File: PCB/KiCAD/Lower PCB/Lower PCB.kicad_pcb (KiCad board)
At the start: 2 copper layers, 179.5 x 163.2 mm, 138 parts, among them IC1 ADG608BRZ, IC2 ADG608BRZ, J1 Conn_01x04, J2 Conn_01x02, J3 Conn_01x08, M1 Conn_01x02_Pin, M2 Conn_01x02_Pin, M3 Conn_01x02_Pin, M4 Conn_01x02_Pin, Q1 SFH320, Q10 SFH320, Q11 SFH320, Q12 SFH320, Q13 SFH320, Q14 SFH320, Q15 SFH320, Q16 SFH320, Q2 SFH320, Q3 SFH320, Q4 SFH320, Q5 SFH320, Q6 SFH320, Q7 SFH320, Q8 SFH320, Q9 SFH320, U1 ATmega328PB-A, U2 LMD18200, U3 LMD18200, U4 LMD18200, U5 LMD18200, U6 ATmega328PB-A, Y1 Crystal_GND24, Y2 Crystal_GND24

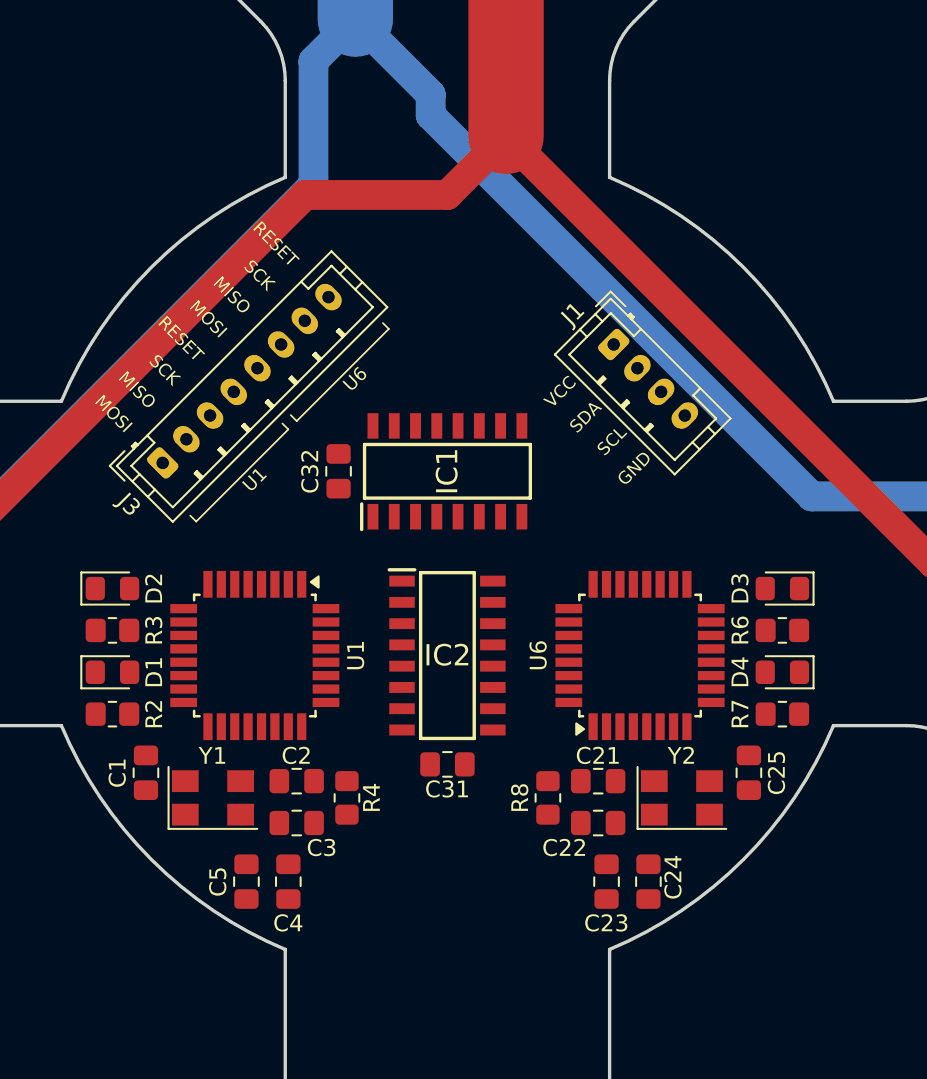
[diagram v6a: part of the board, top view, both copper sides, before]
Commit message: More work to the Main PCB and refinement of Via sizes
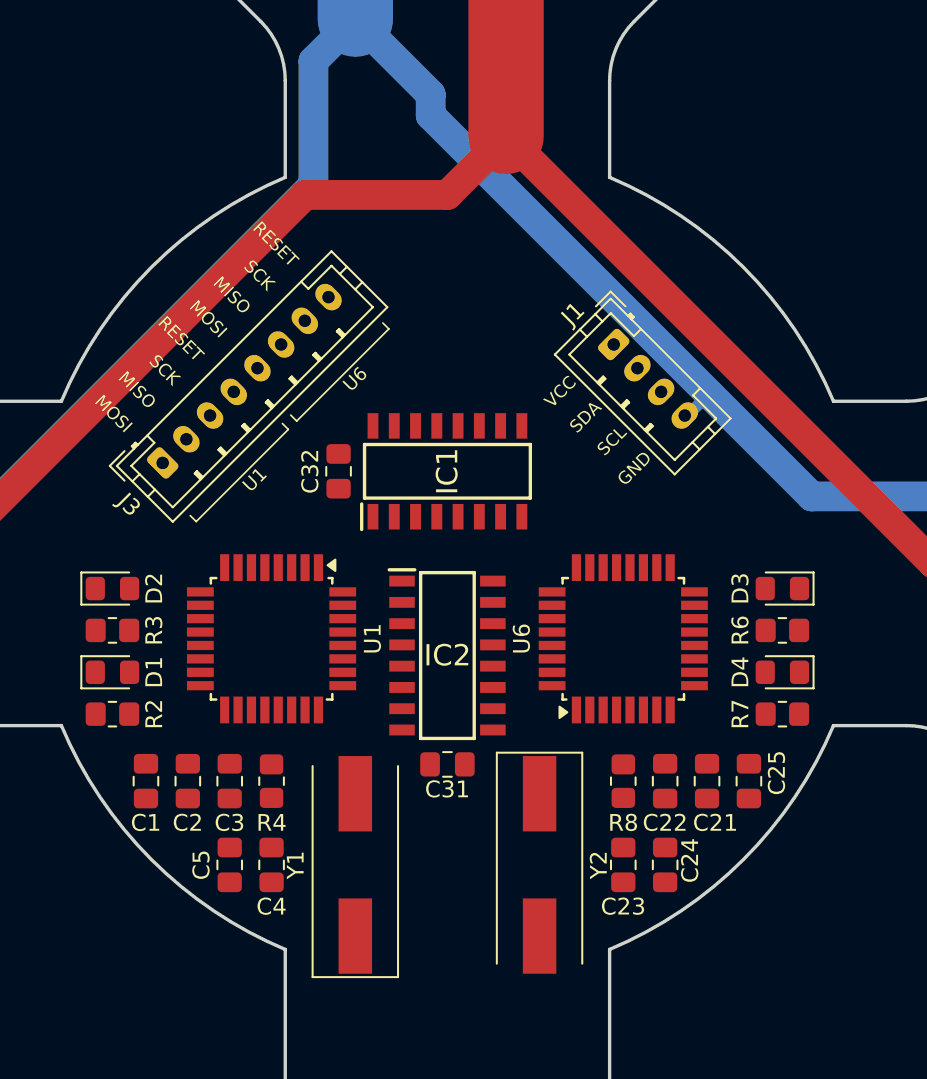
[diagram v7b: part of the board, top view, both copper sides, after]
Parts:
- Y1, Y2: value Crystal_GND24 -> Crystal; footprint Crystal:Crystal_SMD_5032-4Pin_5.0x3.2mm -> Crystal:Crystal_SMD_HC49-SD
- moved Y1 9.39 mm to (-5.50, 18.0), turned to 90 degrees
- moved Y2 9.39 mm to (5.50, 18.0), turned to -90 degrees
- moved C2 6.50 mm to (-15.5, 13.0), turned to 90 degrees
- moved C21 6.50 mm to (15.5, 13.0), turned to -90 degrees
- moved C22 4.72 mm to (13.0, 13.0), turned to -90 degrees
- moved C3 4.72 mm to (-13.0, 13.0), turned to -90 degrees
- moved R4 4.61 mm to (-10.5, 13.0)
- moved R8 4.61 mm to (10.5, 13.0)
- moved C23 1.41 mm to (10.5, 18.0)
- moved C24 1.41 mm to (13.0, 18.0)
- moved C4 1.41 mm to (-10.5, 18.0)
- moved C5 1.41 mm to (-13.0, 18.0)
- moved U1 1.41 mm to (-10.5, 4.50)
- moved U6 1.41 mm to (10.5, 4.50)
- moved C1 0.50 mm to (-18.0, 13.0)
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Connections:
- Y1 pad 1: Net-(U1-XTAL1/PB6) -> Net-(U1-XTAL2/PB7)
- Y1 pad 2: unconnected-(Y1-Pad2) -> Net-(U1-XTAL1/PB6)
- Y2 pad 1: Net-(U6-XTAL1/PB6) -> Net-(U6-XTAL2/PB7)
- Y2 pad 2: unconnected-(Y2-Pad2) -> Net-(U6-XTAL1/PB6)
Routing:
- net MOTOR_1_BRAKE: track 379.0 -> 381.0 mm

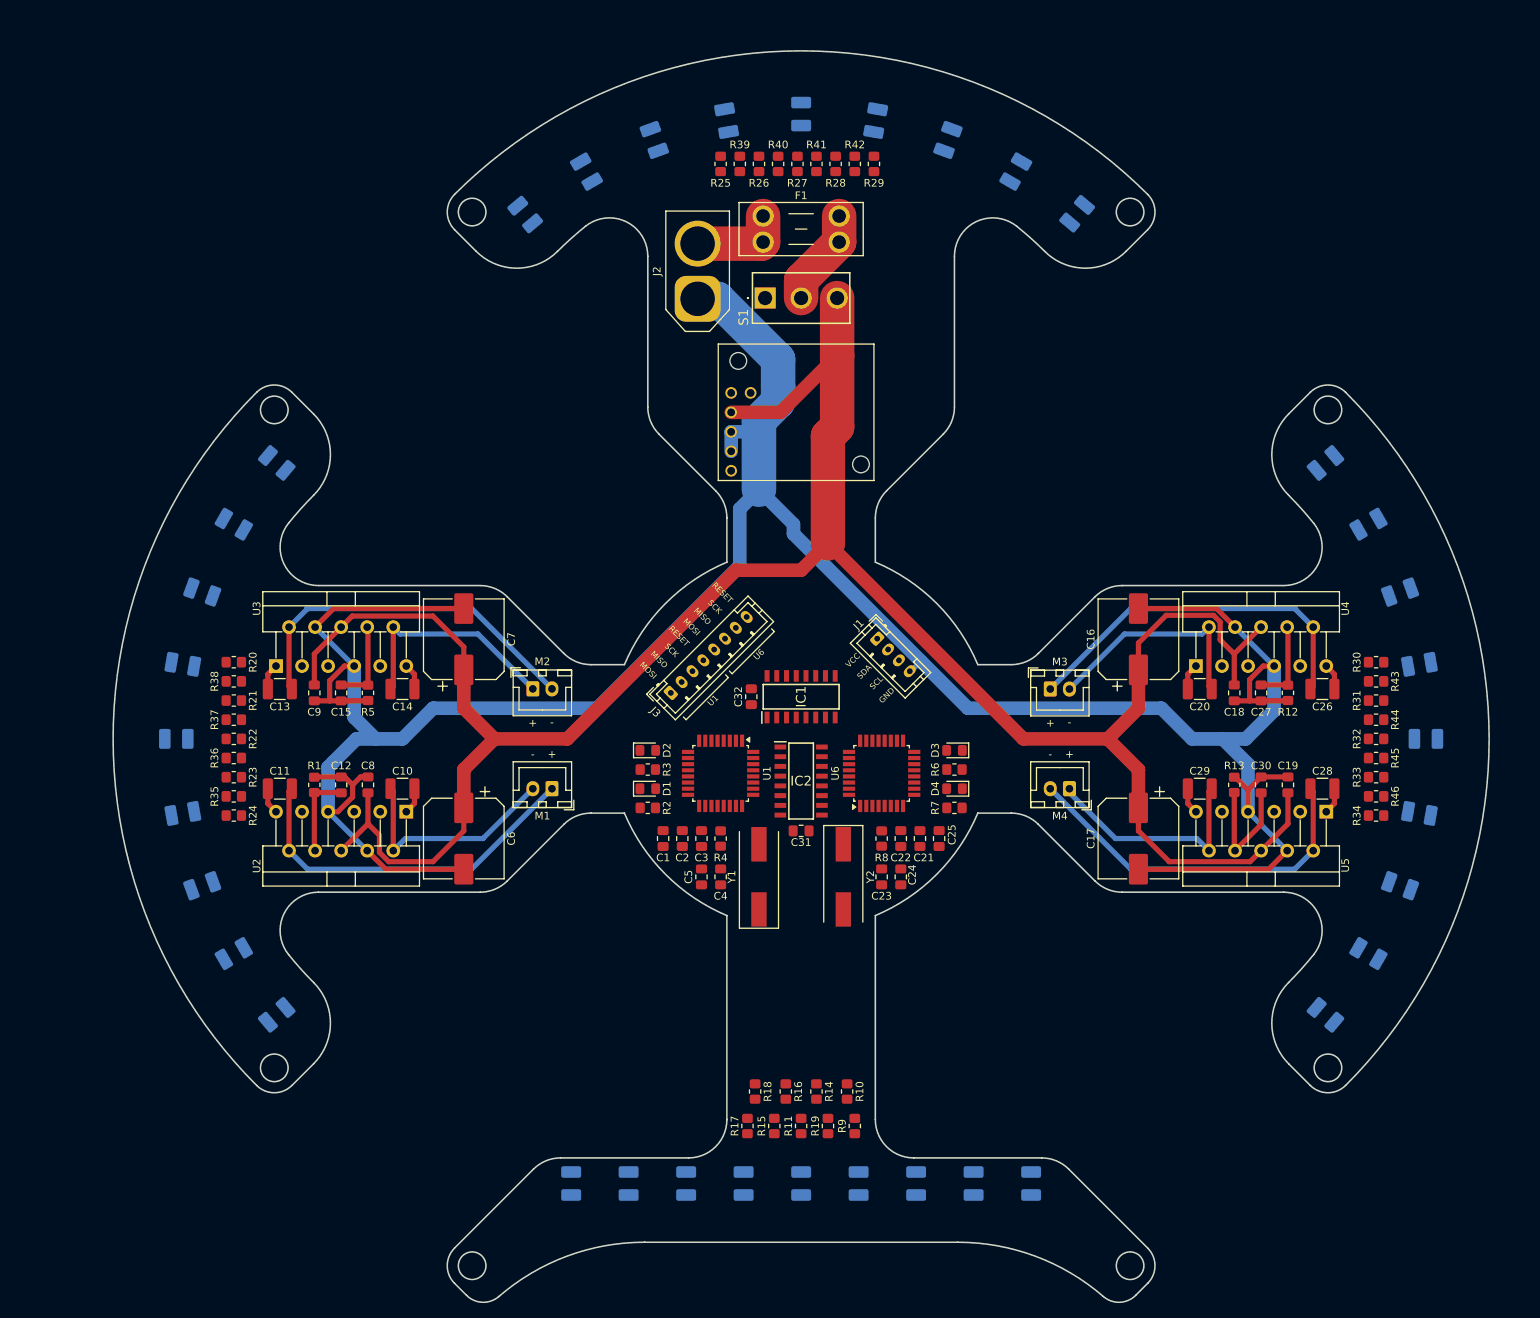
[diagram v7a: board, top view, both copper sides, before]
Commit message: Redone main PCB traces and started lower PCB
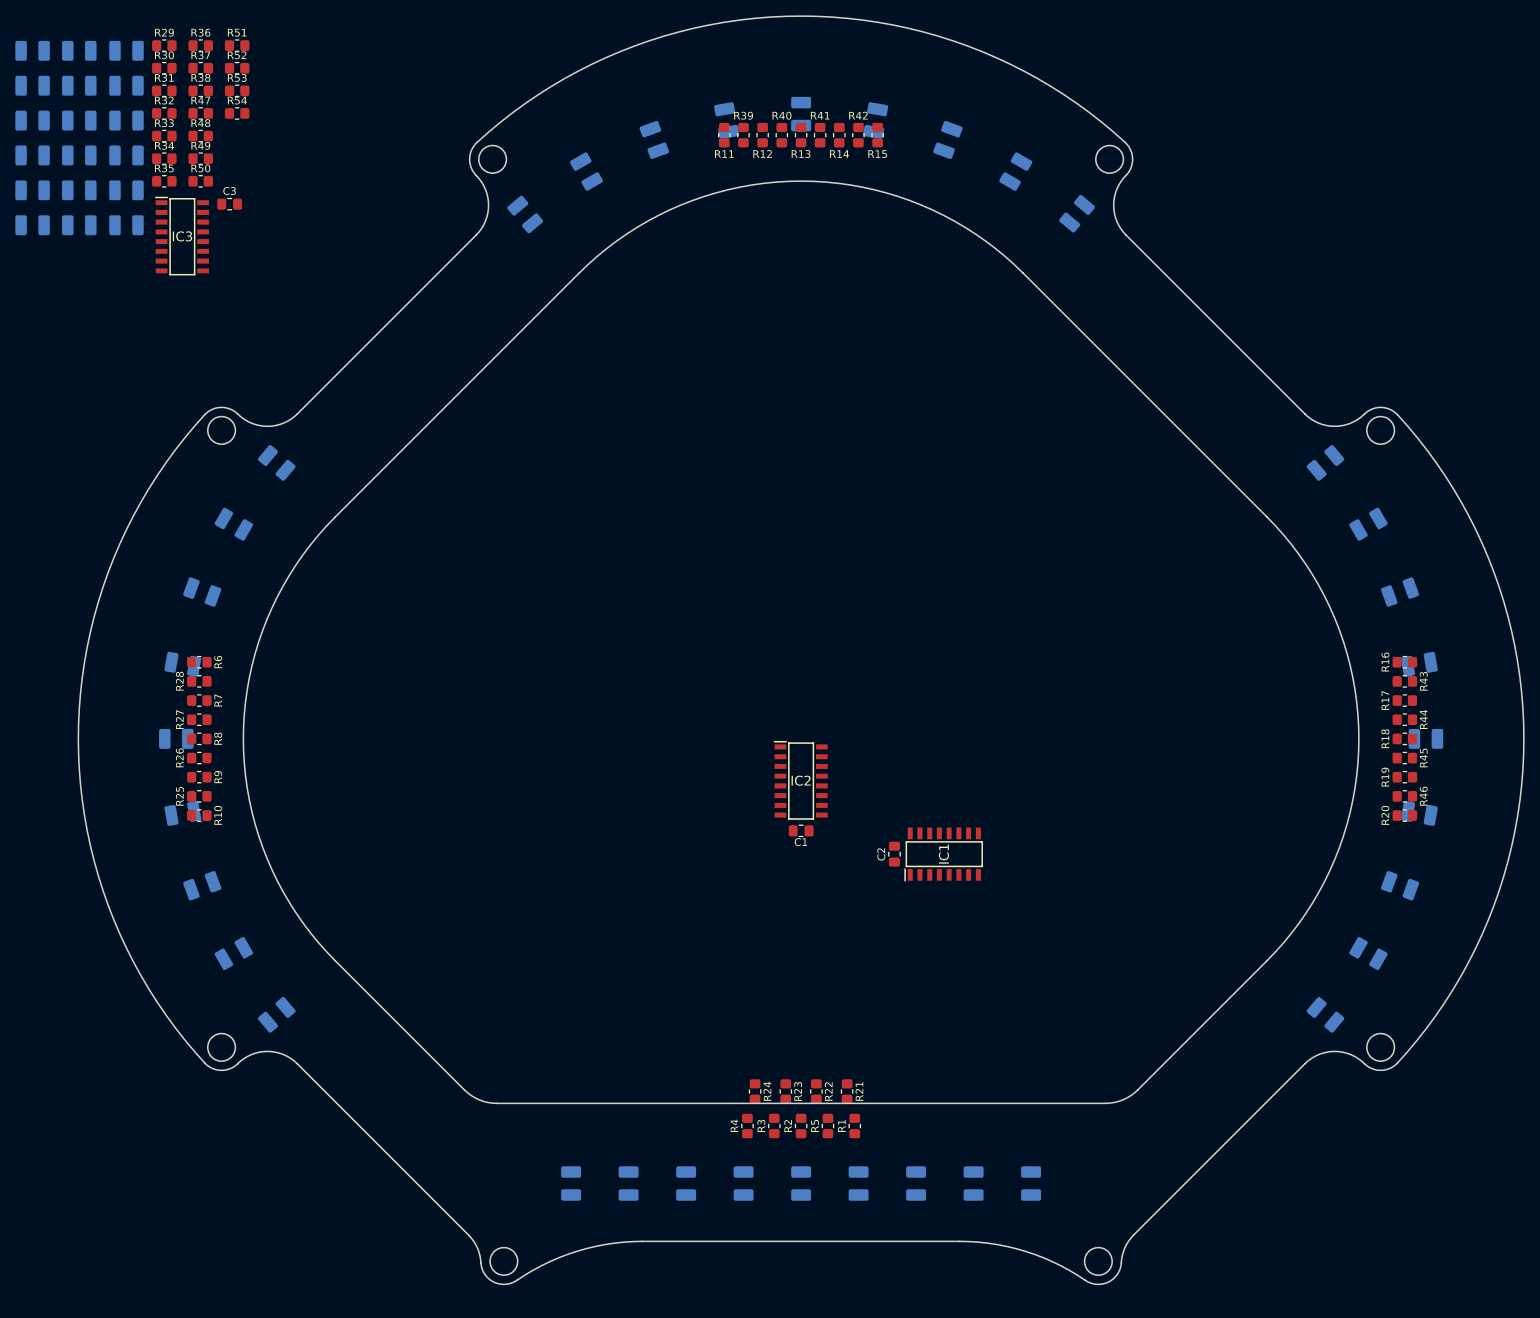
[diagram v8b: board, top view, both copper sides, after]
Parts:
- removed the C1 at (-18.0, 13.0)
- removed C10, C11, C13, C14, C20, C26, C28, C29: 10nF, Capacitor_SMD:C_1210_3225Metric_Pad1.33x2.70mm_HandSolder
- removed C12, C15, C18, C19, C27, C30, C8, C9: 0.1uF, Capacitor_SMD:C_0805_2012Metric_Pad1.18x1.45mm_HandSolder
- removed C16, C17, C6, C7: 220uF, Capacitor_SMD:CP_Elec_10x10
- removed the C2 at (-15.5, 13.0)
- removed C21, C22, C25: 100nF, Capacitor_SMD:C_0805_2012Metric_Pad1.18x1.45mm_HandSolder
- removed C23, C24, C4, C5: 22pF, Capacitor_SMD:C_0805_2012Metric_Pad1.18x1.45mm_HandSolder
- removed the D1 at (-20.0, 6.50)
- removed the D2 at (-20.0, 1.50)
- removed the D3 at (20.0, 1.50)
- removed the D4 at (20.0, 6.50)
- removed F1: Fuse, Fuse:Fuseholder_Blade_Mini_Keystone_3568
- removed J1: Conn_01x04, Connector_JST:JST_PH_B4B-PH-K_1x04_P2.00mm_Vertical
- removed J2: Conn_01x02, Connector_AMASS:AMASS_XT60-M_1x02_P7.20mm_Vertical
- removed J3: Conn_01x08, Connector_JST:JST_PH_B8B-PH-K_1x08_P2.00mm_Vertical
- removed M1, M2, M3, M4: Conn_01x02_Pin, Connector_JST:JST_XH_B2B-XH-A_1x02_P2.50mm_Vertical
- removed the R1 at (-63.5, 6.00)
- removed the R12 at (63.5, -6.00)
- removed the R13 at (56.5, 6.00)
- removed the R2 at (-20.0, 9.00)
- removed the R3 at (-20.0, 4.00)
- removed the R4 at (-10.5, 13.0)
- removed the R5 at (-56.5, -6.00)
- removed the R6 at (20.0, 4.00)
- removed the R7 at (20.0, 9.00)
- removed the R8 at (10.5, 13.0)
- removed S1: 1101M2S3CGE2, 1101M2S3CGE2:1101M2S3CGE2
- removed U1, U6: ATmega328PB-A, Package_QFP:TQFP-32_7x7mm_P0.8mm
- removed U2, U3, U4, U5: LMD18200, Package_TO_SOT_THT:TO-220-11_P3.4x5.08mm_StaggerOdd_Lead4.58mm_Vertical
- removed U7: ~, Pololu:D36V28F5
- removed Y1, Y2: Crystal, Crystal:Crystal_SMD_HC49-SD
- added D21: LED, LED_SMD:LED_PLCC-2_3.4x3.0mm_KA, B.Cu at (-94.2, -89.8)
- added D22: LED, LED_SMD:LED_PLCC-2_3.4x3.0mm_KA, B.Cu at (-94.2, -85.2)
- added D23: LED, LED_SMD:LED_PLCC-2_3.4x3.0mm_KA, B.Cu at (-94.2, -80.7)
- added D24: LED, LED_SMD:LED_PLCC-2_3.4x3.0mm_KA, B.Cu at (-94.2, -76.1)
- added D25: LED, LED_SMD:LED_PLCC-2_3.4x3.0mm_KA, B.Cu at (-94.2, -71.5)
- added D26: LED, LED_SMD:LED_PLCC-2_3.4x3.0mm_KA, B.Cu at (-94.2, -67.0)
- added D27: LED, LED_SMD:LED_PLCC-2_3.4x3.0mm_KA, B.Cu at (-100.2, -89.8)
- added D28: LED, LED_SMD:LED_PLCC-2_3.4x3.0mm_KA, B.Cu at (-100.2, -85.2)
- added D29: LED, LED_SMD:LED_PLCC-2_3.4x3.0mm_KA, B.Cu at (-100.2, -80.7)
- added D30: LED, LED_SMD:LED_PLCC-2_3.4x3.0mm_KA, B.Cu at (-100.2, -76.1)
- added IC3: ADG608BRZ, ADG608BRZ:SOIC127P600X175-16N, F.Cu at (-80.7, -65.5)
- added Q17: SFH320, LED_SMD:LED_PLCC-2_3.4x3.0mm_KA, B.Cu at (-100.2, -71.5)
- added Q18: SFH320, LED_SMD:LED_PLCC-2_3.4x3.0mm_KA, B.Cu at (-100.2, -67.0)
- added Q19: SFH320, LED_SMD:LED_PLCC-2_3.4x3.0mm_KA, B.Cu at (-88.0, -89.8)
- added Q20: SFH320, LED_SMD:LED_PLCC-2_3.4x3.0mm_KA, B.Cu at (-88.0, -85.2)
- added Q21: SFH320, LED_SMD:LED_PLCC-2_3.4x3.0mm_KA, B.Cu at (-88.0, -80.7)
- added Q22: SFH320, LED_SMD:LED_PLCC-2_3.4x3.0mm_KA, B.Cu at (-88.0, -76.1)
- added Q23: SFH320, LED_SMD:LED_PLCC-2_3.4x3.0mm_KA, B.Cu at (-88.0, -71.5)
- added Q24: SFH320, LED_SMD:LED_PLCC-2_3.4x3.0mm_KA, B.Cu at (-88.0, -67.0)
- added R29: 330, Resistor_SMD:R_0805_2012Metric_Pad1.20x1.40mm_HandSolder, F.Cu at (-83.1, -90.4)
- added R30: 330, Resistor_SMD:R_0805_2012Metric_Pad1.20x1.40mm_HandSolder, F.Cu at (-83.1, -87.5)
- added R31: 330, Resistor_SMD:R_0805_2012Metric_Pad1.20x1.40mm_HandSolder, F.Cu at (-83.1, -84.5)
- added R32: 330, Resistor_SMD:R_0805_2012Metric_Pad1.20x1.40mm_HandSolder, F.Cu at (-83.1, -81.6)
- added R33: 330, Resistor_SMD:R_0805_2012Metric_Pad1.20x1.40mm_HandSolder, F.Cu at (-83.1, -78.6)
- added R34: 330, Resistor_SMD:R_0805_2012Metric_Pad1.20x1.40mm_HandSolder, F.Cu at (-83.1, -75.7)
- added R35: 330, Resistor_SMD:R_0805_2012Metric_Pad1.20x1.40mm_HandSolder, F.Cu at (-83.1, -72.7)
- added R36: 330, Resistor_SMD:R_0805_2012Metric_Pad1.20x1.40mm_HandSolder, F.Cu at (-78.3, -90.4)
- added R37: 330, Resistor_SMD:R_0805_2012Metric_Pad1.20x1.40mm_HandSolder, F.Cu at (-78.3, -87.5)
- added R38: 330, Resistor_SMD:R_0805_2012Metric_Pad1.20x1.40mm_HandSolder, F.Cu at (-78.3, -84.5)
- added R47: 10k, Resistor_SMD:R_0805_2012Metric_Pad1.20x1.40mm_HandSolder, F.Cu at (-78.3, -81.6)
- added R48: 10k, Resistor_SMD:R_0805_2012Metric_Pad1.20x1.40mm_HandSolder, F.Cu at (-78.3, -78.6)
- added R49: 10k, Resistor_SMD:R_0805_2012Metric_Pad1.20x1.40mm_HandSolder, F.Cu at (-78.3, -75.7)
- added R50: 10k, Resistor_SMD:R_0805_2012Metric_Pad1.20x1.40mm_HandSolder, F.Cu at (-78.3, -72.7)
- added R51: 10k, Resistor_SMD:R_0805_2012Metric_Pad1.20x1.40mm_HandSolder, F.Cu at (-73.6, -90.4)
- added R52: 10k, Resistor_SMD:R_0805_2012Metric_Pad1.20x1.40mm_HandSolder, F.Cu at (-73.6, -87.5)
- added R53: 10k, Resistor_SMD:R_0805_2012Metric_Pad1.20x1.40mm_HandSolder, F.Cu at (-73.6, -84.5)
- added R54: 10k, Resistor_SMD:R_0805_2012Metric_Pad1.20x1.40mm_HandSolder, F.Cu at (-73.6, -81.6)
- moved C3 103.1 mm to (-74.5, -69.8), turned to 0 degrees
- moved C2 27.8 mm to (12.2, 15.0)
- moved IC1 27.8 mm to (18.7, 15.0)
- moved R10 4.50 mm to (-78.5, 10.0)
- moved R25 4.50 mm to (-78.5, 7.50)
- moved R26 4.50 mm to (-78.5, 2.50)
- moved R27 4.50 mm to (-78.5, -2.50)
- moved R28 4.50 mm to (-78.5, -7.50)
- moved R6 4.50 mm to (-78.5, -10.0)
- moved R7 4.50 mm to (-78.5, -5.00)
- moved R8 4.50 mm to (-78.5, 0.00)
- moved R9 4.50 mm to (-78.5, 5.00)
- moved R11 3.78 mm to (-10.0, -78.8)
- moved R12 3.78 mm to (-5.02, -78.8)
- moved R13 3.78 mm to (0.00, -78.8)
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- renumbered C31 to C1, C32 to C2, D5 to D1, D14 to D10, D15 to D11, D16 to D12, D17 to D13, D18 to D14, D19 to D15, D20 to D16, D21 to D17, D22 to D18, D23 to D19, D6 to D2, D24 to D20, D7 to D3, D8 to D4, D9 to D5, D10 to D6, D11 to D7, D12 to D8, D13 to D9, R9 to R1, R24 to R10, R25 to R11, R26 to R12, R27 to R13, R28 to R14, R29 to R15, R30 to R16, R31 to R17, R32 to R18, R33 to R19, R11 to R2, R34 to R20, R10 to R21, R14 to R22, R16 to R23, R18 to R24, R35 to R25, R36 to R26, R37 to R27, R38 to R28, R15 to R3, R17 to R4, R19 to R5, R20 to R6, R21 to R7, R22 to R8, R23 to R9
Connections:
- C1 pad 2: MOTOR_1_BRAKE -> GND
- C2 pad 2: MOTOR_1_BRAKE -> GND
- C3 pad 1: MOTOR_1_BRAKE -> +5V
- C3 pad 2: +5V -> GND
- D1 pad 1: MOTOR_1_BRAKE -> GND
- D10 pad 1: MOTOR_1_BRAKE -> GND
- D11 pad 1: MOTOR_1_BRAKE -> GND
- D12 pad 1: MOTOR_1_BRAKE -> GND
- D13 pad 1: MOTOR_1_BRAKE -> GND
- D14 pad 1: MOTOR_1_BRAKE -> GND
- D15 pad 1: MOTOR_1_BRAKE -> GND
- D16 pad 1: MOTOR_1_BRAKE -> GND
- D17 pad 1: MOTOR_1_BRAKE -> GND
- D18 pad 1: MOTOR_1_BRAKE -> GND
- D19 pad 1: MOTOR_1_BRAKE -> GND
- D2 pad 1: MOTOR_1_BRAKE -> GND
- D20 pad 1: MOTOR_1_BRAKE -> GND
- D3 pad 1: MOTOR_1_BRAKE -> GND
- D4 pad 1: MOTOR_1_BRAKE -> GND
- D5 pad 1: MOTOR_1_BRAKE -> GND
- D6 pad 1: MOTOR_1_BRAKE -> GND
- D7 pad 1: MOTOR_1_BRAKE -> GND
- D8 pad 1: MOTOR_1_BRAKE -> GND
- D9 pad 1: MOTOR_1_BRAKE -> GND
- IC1 pad 14: MOTOR_1_BRAKE -> GND
- IC1 pad 3: MOTOR_1_BRAKE -> GND
- IC2 pad 14: MOTOR_1_BRAKE -> GND
- IC2 pad 3: MOTOR_1_BRAKE -> GND
- R21 pad 1: MOTOR_1_BRAKE -> GND
- R22 pad 1: MOTOR_1_BRAKE -> GND
- R23 pad 1: MOTOR_1_BRAKE -> GND
- R24 pad 1: MOTOR_1_BRAKE -> GND
- R25 pad 1: MOTOR_1_BRAKE -> GND
- R26 pad 1: MOTOR_1_BRAKE -> GND
- R27 pad 1: MOTOR_1_BRAKE -> GND
- R28 pad 1: MOTOR_1_BRAKE -> GND
- R39 pad 1: MOTOR_1_BRAKE -> GND
- R40 pad 1: MOTOR_1_BRAKE -> GND
- R41 pad 1: MOTOR_1_BRAKE -> GND
- R42 pad 1: MOTOR_1_BRAKE -> GND
- R43 pad 1: MOTOR_1_BRAKE -> GND
- R44 pad 1: MOTOR_1_BRAKE -> GND
- R45 pad 1: MOTOR_1_BRAKE -> GND
- R46 pad 1: MOTOR_1_BRAKE -> GND
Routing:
- net MOTOR_1_BRAKE: track 381.0 -> 0.00 mm
- net +12V: track 313.1 -> 0.00 mm
- net Net-(M3-Pin_1): track 48.0 -> 0.00 mm
- net Net-(M2-Pin_2): track 47.9 -> 0.00 mm
- net Net-(M4-Pin_2): track 47.9 -> 0.00 mm
- net Net-(M1-Pin_1): track 47.9 -> 0.00 mm
- net Net-(M4-Pin_1): track 30.1 -> 0.00 mm
- net Net-(M1-Pin_2): track 29.8 -> 0.00 mm
- net Net-(M3-Pin_2): track 29.8 -> 0.00 mm
- net Net-(M2-Pin_1): track 29.8 -> 0.00 mm
- net Net-(U5-CURRENT_SENSE_OUTPUT): track 16.6 -> 0.00 mm
- net Net-(S1-COM): track 12.8 -> 0.00 mm
- net Net-(J2-Pin_2): track 12.0 -> 0.00 mm
- net Net-(U4-CURRENT_SENSE_OUTPUT): track 11.1 -> 0.00 mm
- net Net-(U3-CURRENT_SENSE_OUTPUT): track 11.1 -> 0.00 mm
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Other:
- board size 179.5 x 163.2 mm -> 188.6 x 165.4 mm
- board text removed: "+"
- board text removed: "-"
- board text removed: "GND"
- board text removed: "MISO"
- board text removed: "MOSI"
- board text removed: "RESET"
- board text removed: "SCK"
- board text removed: "SCL"
- board text removed: "SDA"
- board text removed: "U1"
- board text removed: "U6"
- board text removed: "VCC"
